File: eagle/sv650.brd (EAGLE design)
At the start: 54.2 x 52.1 mm, 17 parts, among them IC1 7805T

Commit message: improve board layout and update resistor divider circuit
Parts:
- removed U$2: BZT52C20-7-F 20V, SparkFun:SOD-323
- added D5: 16V zener, adafruit:SOD-123
- R5: value 4.7k -> 3.24k
- R6: value 1.2k -> 1k
- moved R4 4.58 mm to (3.05, 41.1)
- moved U$1 0.36 mm to (1.78, 0.51)
- moved _1 0.25 mm to (38.9, 13.2)
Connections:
- net +12V: now also D5.C; no longer U$2.1
- net N$1: now also D5.A; no longer U$2.2
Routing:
- net N$9: track 34.8 -> 31.6 mm
- net R2: track 7.50 -> 9.14 mm
- net N$5: track 22.2 -> 23.8 mm
- net 5V: track 131.1 -> 130.1 mm
- net N$1: track 20.7 -> 19.9 mm

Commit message: add .gitignore Update schema and board with updated connector, resistors for voltage divider and zener.
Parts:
- D5: value 16V zener -> 15V zener
- R5: value 3.24k -> 32.4k
- R6: value 1k -> 10k
- moved D5 0.80 mm to (18.8, 18.8)
- moved D1 0.25 mm to (26.7, 45.5)
- moved D4 0.25 mm to (10.2, 45.5)
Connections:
- net VOLT renamed ADC
- removed net N$1: D5.A, U$3.P$7
- net +12V: now also U$3.P$7
- net GND: now also D5.A, _1.GRND1
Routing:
- net +12V: track 41.0 -> 62.1 mm
- net N$1: track 19.9 -> 0.00 mm
- net GND: track 116.8 -> 136.7 mm
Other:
- board text added: "S/N:"
- board text added: "SV650 ECU Decoder 4.0 http://synfin.net/sv650ecu"

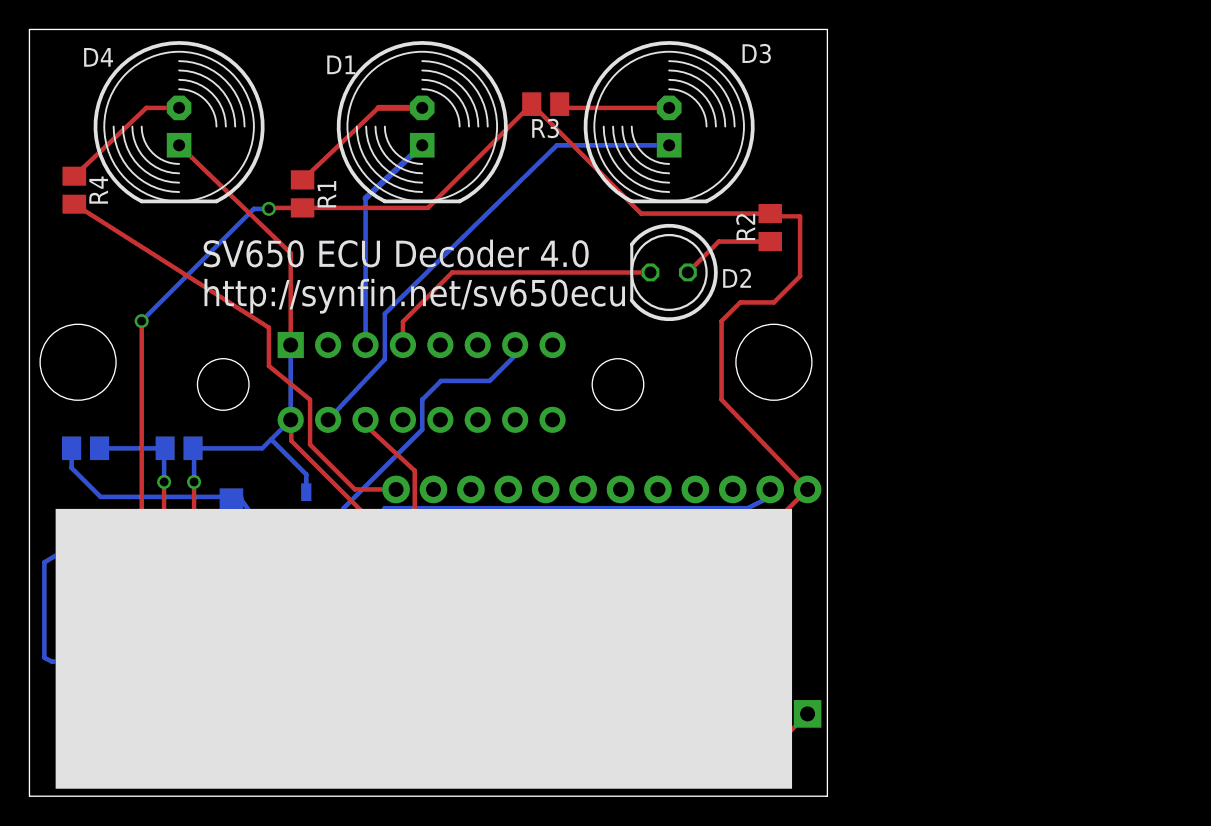
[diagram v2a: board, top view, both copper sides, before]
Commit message: update layout of 7805 to use a pad for solder not drill hole for hard mounting.  Update silkscreen and improve layout for sending to OshPark for fabrication.
Just waiting on feedback on voltage divider & zener.
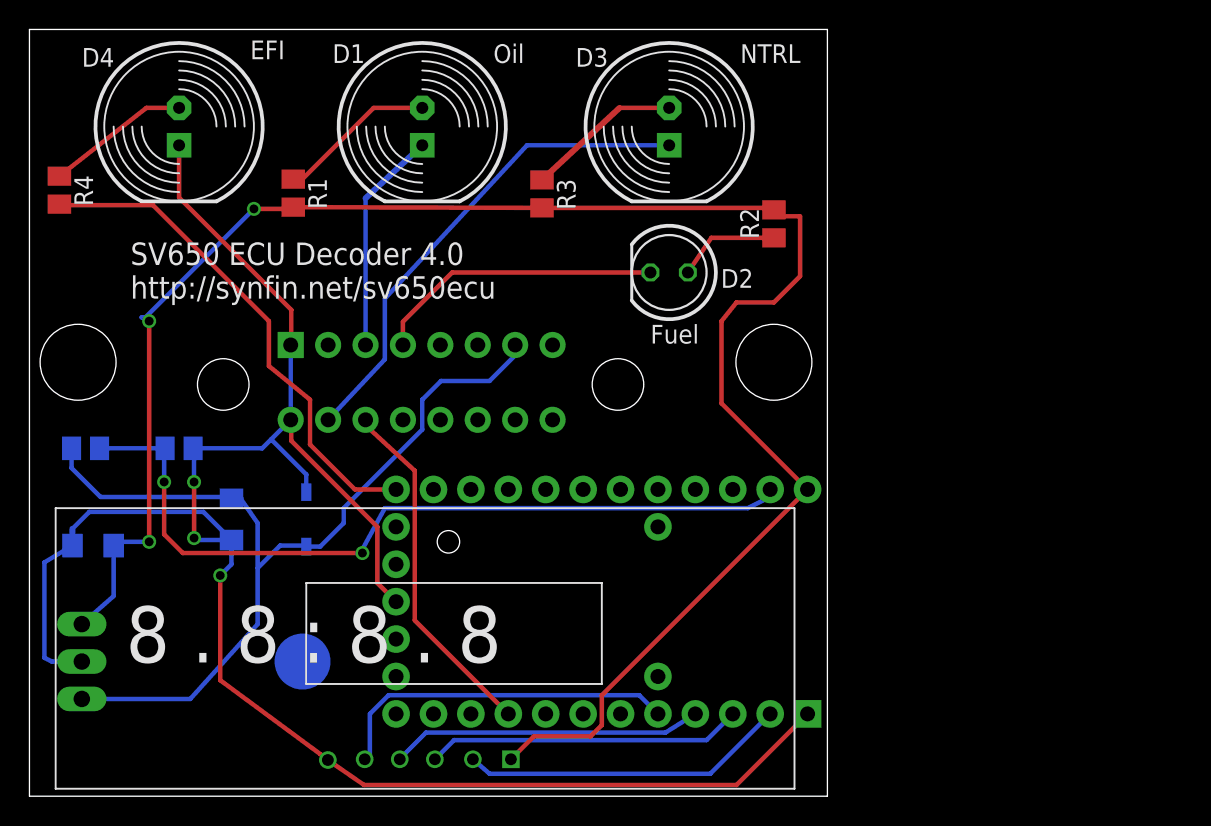
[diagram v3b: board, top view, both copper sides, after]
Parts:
- added U$5: (no value), synfinatic:STANDOFF
- IC1: value 7805T -> 7805; device linear:TO220H -> linear:TO22H-2
- moved R3 6.10 mm to (34.8, 40.9), turned to 270 degrees
- moved IC1 2.79 mm to (11.2, 9.14)
- moved R4 1.02 mm to (2.03, 41.1)
- moved R1 0.64 mm to (17.9, 40.9)
- moved R2 0.36 mm to (50.5, 38.9)
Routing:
- net N$6: track 7.54 -> 10.6 mm
- net 5V: track 130.1 -> 127.3 mm
- net N$9: track 32.0 -> 34.3 mm
- net NTRL: track 32.7 -> 33.6 mm
- net R2: track 8.96 -> 9.73 mm
- net N$8: track 10.1 -> 10.8 mm
- net +12V: track 62.1 -> 62.8 mm
- net N$7: track 6.46 -> 7.09 mm
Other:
- board text added: "EFI"
- board text added: "Fuel"
- board text added: "NTRL"
- board text added: "Oil"

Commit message: board as ordered from OshPark for v4.0
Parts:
- removed D5: 15V zener, adafruit:SOD-123
- added D6: 12V zener, adafruit:SOD-123
- added R8: 10k, resistor:M0805
- C1, C2: device SparkFun:EIA3216 -> adafruit:C025-024X044
- R5: value 32.4k -> 22k
- moved C2 12.7 mm to (15.0, 10.2)
- moved IC1 4.26 mm to (7.11, 10.4), turned to 0 degrees
- moved C1 3.03 mm to (15.7, 21.0), turned to 180 degrees
- moved R5 2.52 mm to (2.83, 21.3), flipped to the top, turned to 270 degrees
- moved R6 0.51 mm to (9.88, 23.2), flipped to the top, turned to 270 degrees
- moved U$1 0.25 mm to (2.03, 0.51)
- moved _1 0.08 mm to (38.8, 13.2)
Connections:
- new net N$13: D6.C, R5.2, R8.1
- net +12V: now also C1.1, R8.2; no longer C1.A, D5.C, R5.2
- net 5V: now also C2.1; no longer C2.A
- net GND: now also C1.2, C2.2, D6.A; no longer C1.C, C2.C, D5.A
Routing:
- net N$13: track 0.00 -> 14.9 mm
- net +12V: track 62.8 -> 55.4 mm, vias 0 -> 1
- net ADC: track 54.6 -> 57.8 mm, vias 2 -> 1
- net 5V: track 127.3 -> 125.5 mm, vias 3 -> 1
- net GND: track 136.4 -> 134.8 mm, vias 3 -> 1

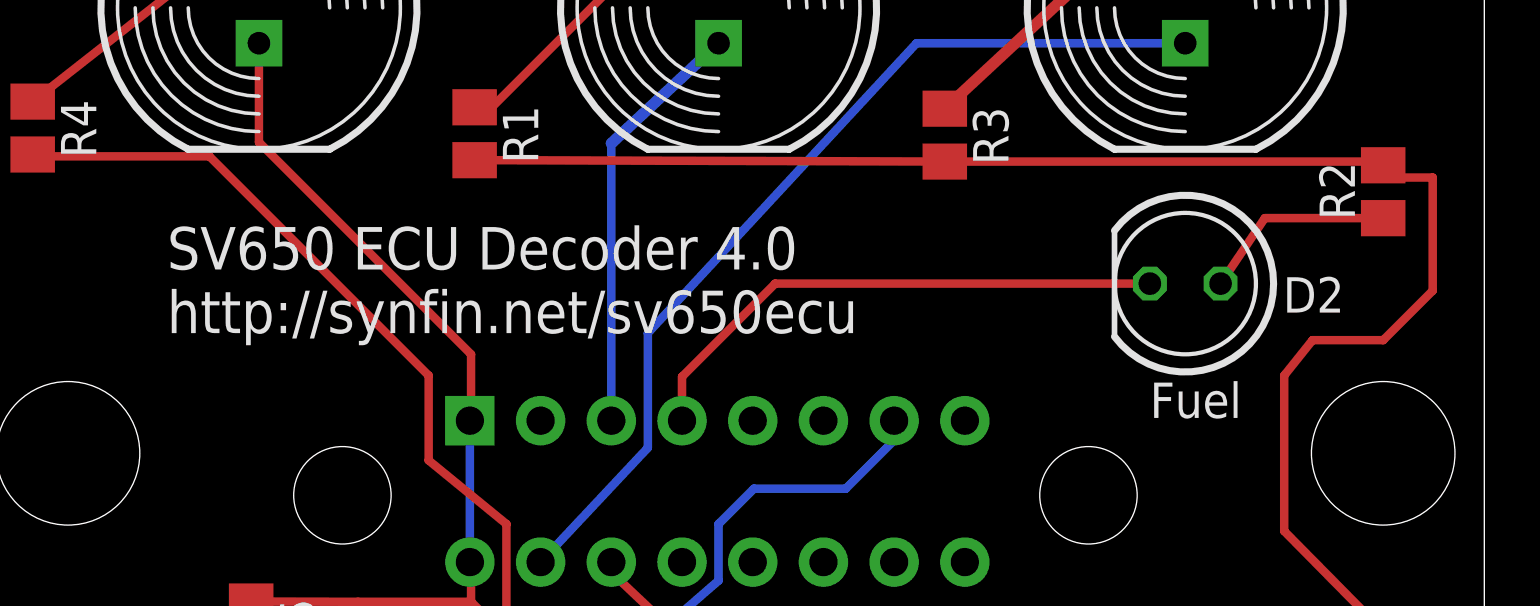
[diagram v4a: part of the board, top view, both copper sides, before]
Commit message: Move fuel LED down to have bigger gap to neutral light rev board to 4.1 add date code to board top silk
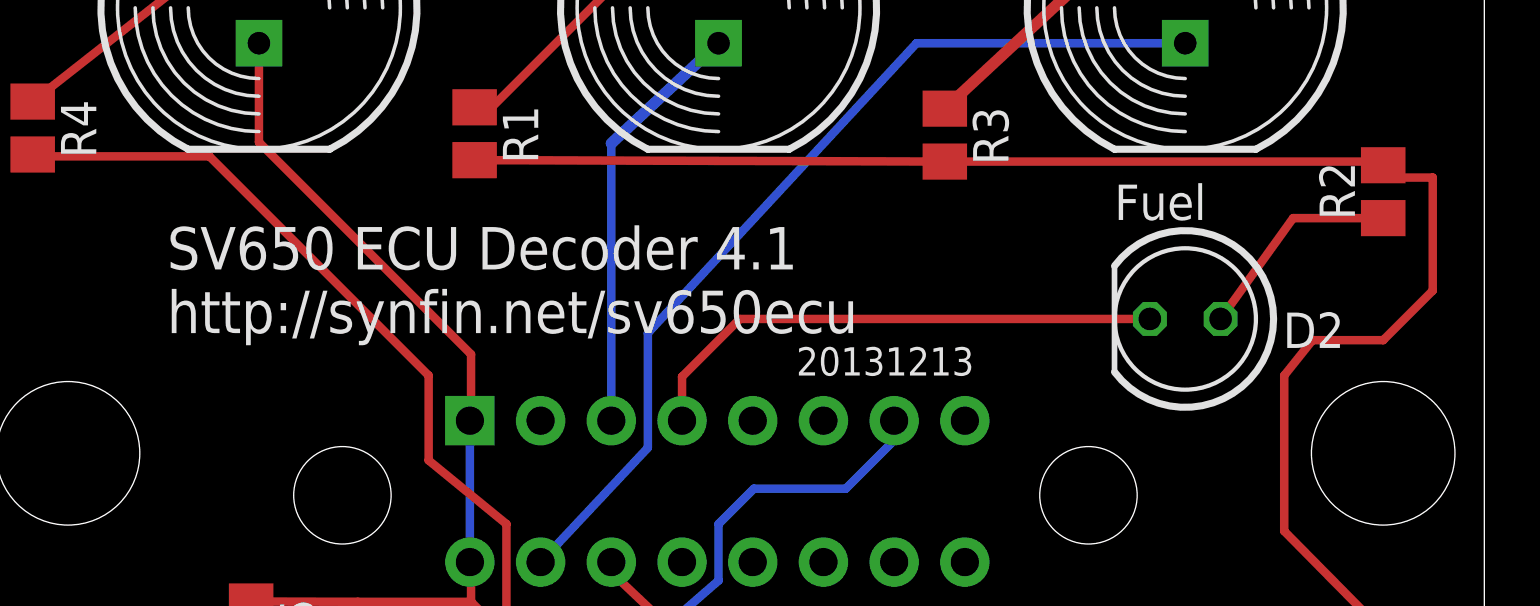
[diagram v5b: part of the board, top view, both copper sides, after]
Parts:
- moved D2 1.27 mm to (43.4, 34.3)
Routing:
- net N$7: track 7.09 -> 7.70 mm
- net FUEL: track 19.8 -> 19.2 mm
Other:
- board text added: "20131213"
- board text added: "SV650 ECU Decoder 4.1 http://synfin.net/sv650ecu"
- board text removed: "SV650 ECU Decoder 4.0 http://synfin.net/sv650ecu"
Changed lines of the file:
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@@
 <hole x="3.302" y="29.464" drill="5.1562"/>
 <hole x="50.546" y="29.464" drill="5.1562"/>
-<text x="6.858" y="33.782" size="1.524" layer="21" font="vector">SV650 ECU Decoder 4.0
+<text x="6.858" y="33.782" size="1.524" layer="21" font="vector">SV650 ECU Decoder 4.1
 http://synfin.net/sv650ecu</text>
 <text x="53.594" y="49.022" size="1.778" layer="22" rot="MR0">S/N:</text>
@@
 <text x="31.496" y="49.784" size="1.27" layer="112">Oil</text>
 <text x="48.26" y="49.784" size="1.27" layer="112">NTRL</text>
-<text x="42.164" y="30.734" size="1.27" layer="112">Fuel</text>
+<text x="40.894" y="37.846" size="1.27" layer="112">Fuel</text>
+<text x="29.464" y="32.258" size="1.016" layer="21">20131213</text>
 </plain>
 <attributes>
@@
 <attribute name="MPN" value="" x="43.434" y="45.466" size="1.778" layer="27" rot="R270" display="off"/>
 </element>
-<element name="D2" library="led" package="LED5MM" value="Blue" x="43.434" y="35.56" smashed="yes" rot="R180">
-<attribute name="NAME" x="49.149" y="35.7886" size="1.27" layer="25" ratio="10" rot="R180"/>
-<attribute name="OC_NEWARK" value="unknown" x="43.434" y="35.56" size="1.778" layer="27" rot="R180" display="off"/>
-<attribute name="MF" value="" x="43.434" y="35.56" size="1.778" layer="27" rot="R180" display="off"/>
-<attribute name="MPN" value="" x="43.434" y="35.56" size="1.778" layer="27" rot="R180" display="off"/>
+<element name="D2" library="led" package="LED5MM" value="Blue" x="43.434" y="34.29" smashed="yes" rot="R180">
+<attribute name="NAME" x="49.149" y="34.5186" size="1.27" layer="25" ratio="10" rot="R180"/>
+<attribute name="OC_NEWARK" value="unknown" x="43.434" y="34.29" size="1.778" layer="27" rot="R180" display="off"/>
+<attribute name="MF" value="" x="43.434" y="34.29" size="1.778" layer="27" rot="R180" display="off"/>
+<attribute name="MPN" value="" x="43.434" y="34.29" size="1.778" layer="27" rot="R180" display="off"/>
 </element>
 <element name="R4" library="resistor" package="M0805" value="150" x="2.032" y="41.148" smashed="yes" rot="R270">
@@
 <contactref element="R2" pad="1"/>
 <contactref element="D2" pad="A"/>
-<wire x1="44.704" y1="35.56" x2="46.294" y2="37.912" width="0.3048" layer="1"/>
-<wire x1="46.294" y1="37.912" x2="50.546" y2="37.912" width="0.3048" layer="1"/>
+<wire x1="44.704" y1="34.29" x2="47.31" y2="37.912" width="0.3048" layer="1"/>
+<wire x1="47.31" y1="37.912" x2="50.546" y2="37.912" width="0.3048" layer="1"/>
 </signal>
 <signal name="N$9">
@@
 <contactref element="D2" pad="K"/>
 <contactref element="U$3" pad="P$4"/>
-<wire x1="42.164" y1="35.56" x2="28.702" y2="35.56" width="0.3048" layer="1"/>
-<wire x1="28.702" y1="35.56" x2="25.358" y2="32.216" width="0.3048" layer="1"/>
+<wire x1="42.164" y1="34.29" x2="27.432" y2="34.29" width="0.3048" layer="1"/>
+<wire x1="27.432" y1="34.29" x2="25.358" y2="32.216" width="0.3048" layer="1"/>
 <wire x1="25.358" y1="32.216" x2="25.358" y2="30.636" width="0.3048" layer="1"/>
 </signal>

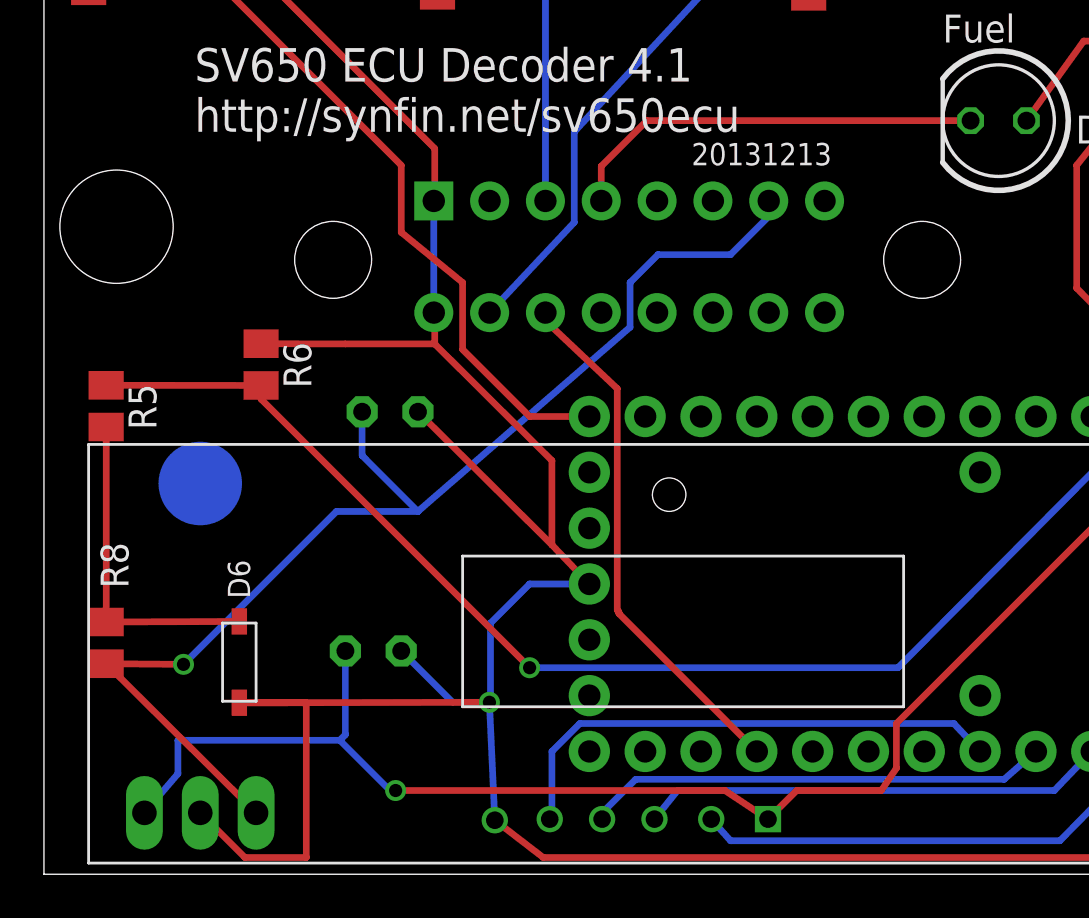
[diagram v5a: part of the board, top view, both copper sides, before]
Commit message: update board & schema to v4.1 - Add 5V zener to protect ADC from shorts - Add .1uF cap to even out ADC line from noise - Tweak placement of low fuel LED - Tweak placement of S/N: XXXXXX
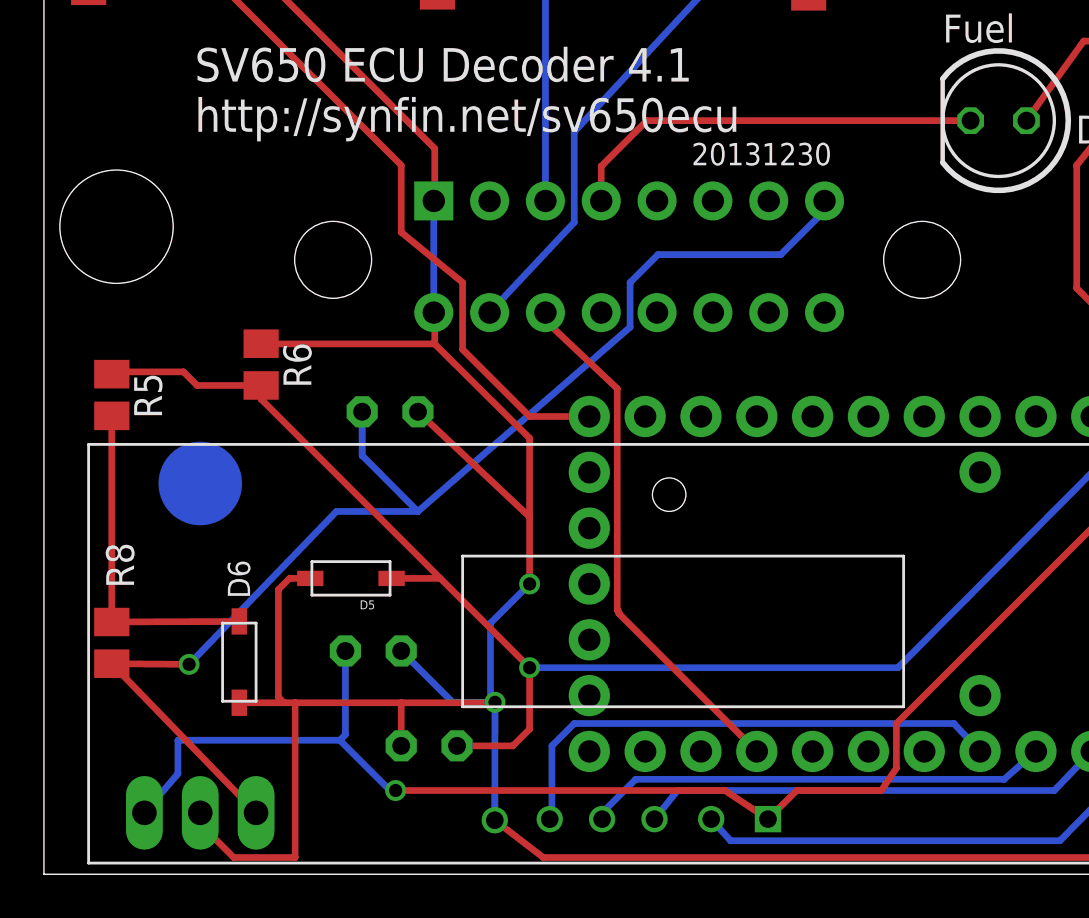
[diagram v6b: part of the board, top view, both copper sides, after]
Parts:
- added C3: .1uF, adafruit:C025-024X044
- added D5: 5V zener, adafruit:SOD-123
- D6: value 12V zener -> 20V zener
- moved R5 0.57 mm to (3.09, 21.8)
- moved R8 0.25 mm to (3.09, 10.5)
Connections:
- net +12V: now also U$3.P$8; no longer U$3.P$7
- net ADC: now also C3.1, D5.C
- net GND: now also C3.2, D5.A; no longer _1.GRND1
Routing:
- net ADC: track 57.8 -> 66.7 mm
- net +12V: track 55.4 -> 57.4 mm
- net GND: track 134.8 -> 135.6 mm, vias 1 -> 2
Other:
- board text added: "20131230"
- board text removed: "20131213"
